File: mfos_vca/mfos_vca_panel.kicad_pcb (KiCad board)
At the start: 2 copper layers, 50.5 x 128.5 mm, 8 parts

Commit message: Finalize panel and pcb for VCA, add gerbers
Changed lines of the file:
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@@
 			(outputformat 1)
 			(mirror no)
-			(drillshape 1)
+			(drillshape 0)
 			(scaleselection 1)
-			(outputdirectory "")
+			(outputdirectory "panel_gerbers/")
 		)
 	)
@@
 	)
 	(gr_line
-		(start 120.883706 91.75)
-		(end 156.183706 91.75)
+		(start 118 91.75)
+		(end 159 91.75)
 		(stroke
 			(width 0.2)

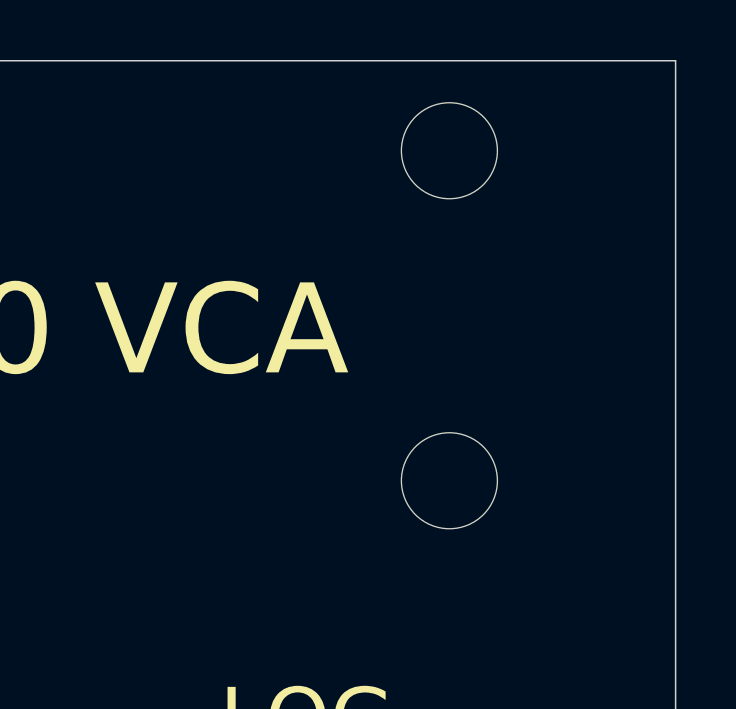
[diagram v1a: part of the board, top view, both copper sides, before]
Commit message: fix pcb holes
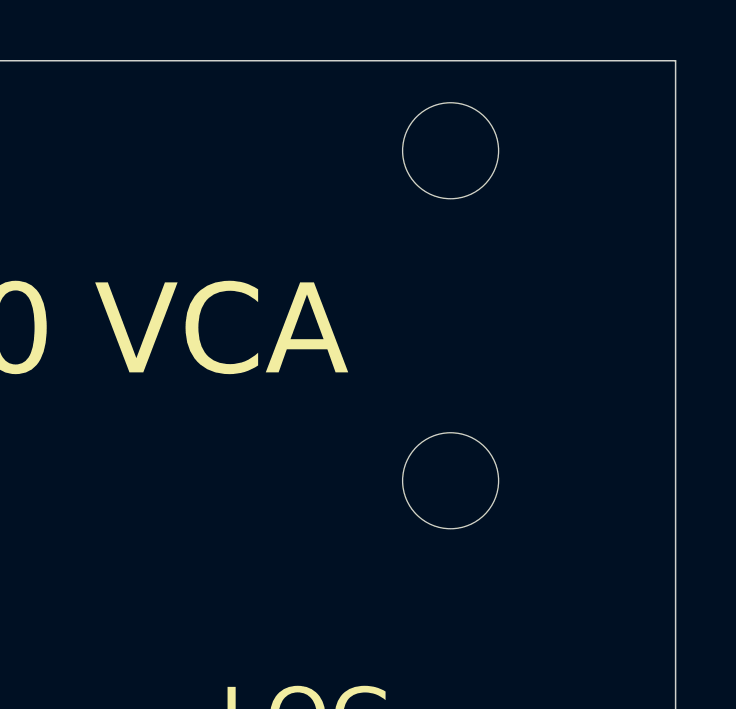
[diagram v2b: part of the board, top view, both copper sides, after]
